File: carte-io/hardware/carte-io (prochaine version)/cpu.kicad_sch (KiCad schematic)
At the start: 24 parts, among them J3 FTSH-105-01-L-DH, SW1 SW_Push, SW2 SW_Push, U1 STM32U545VETx, X1 ASE-16.000MHZ-LC-T

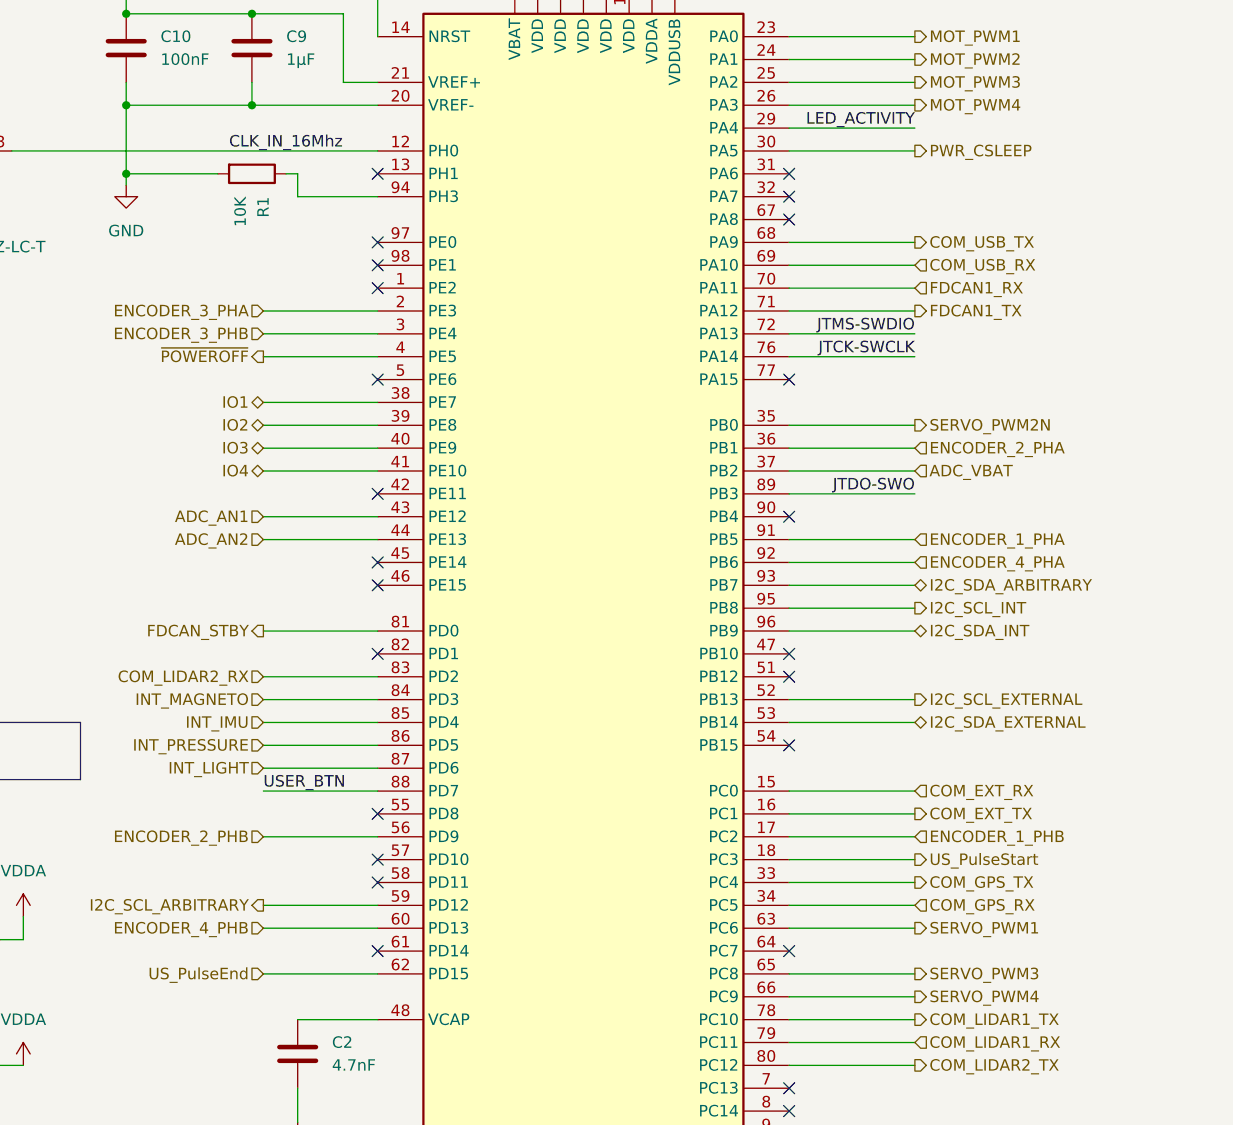
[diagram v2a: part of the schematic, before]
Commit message: WIP ajout du driver uart (marche) et du driver I2C (juste generé par chatgpt, à reprendre et tester)
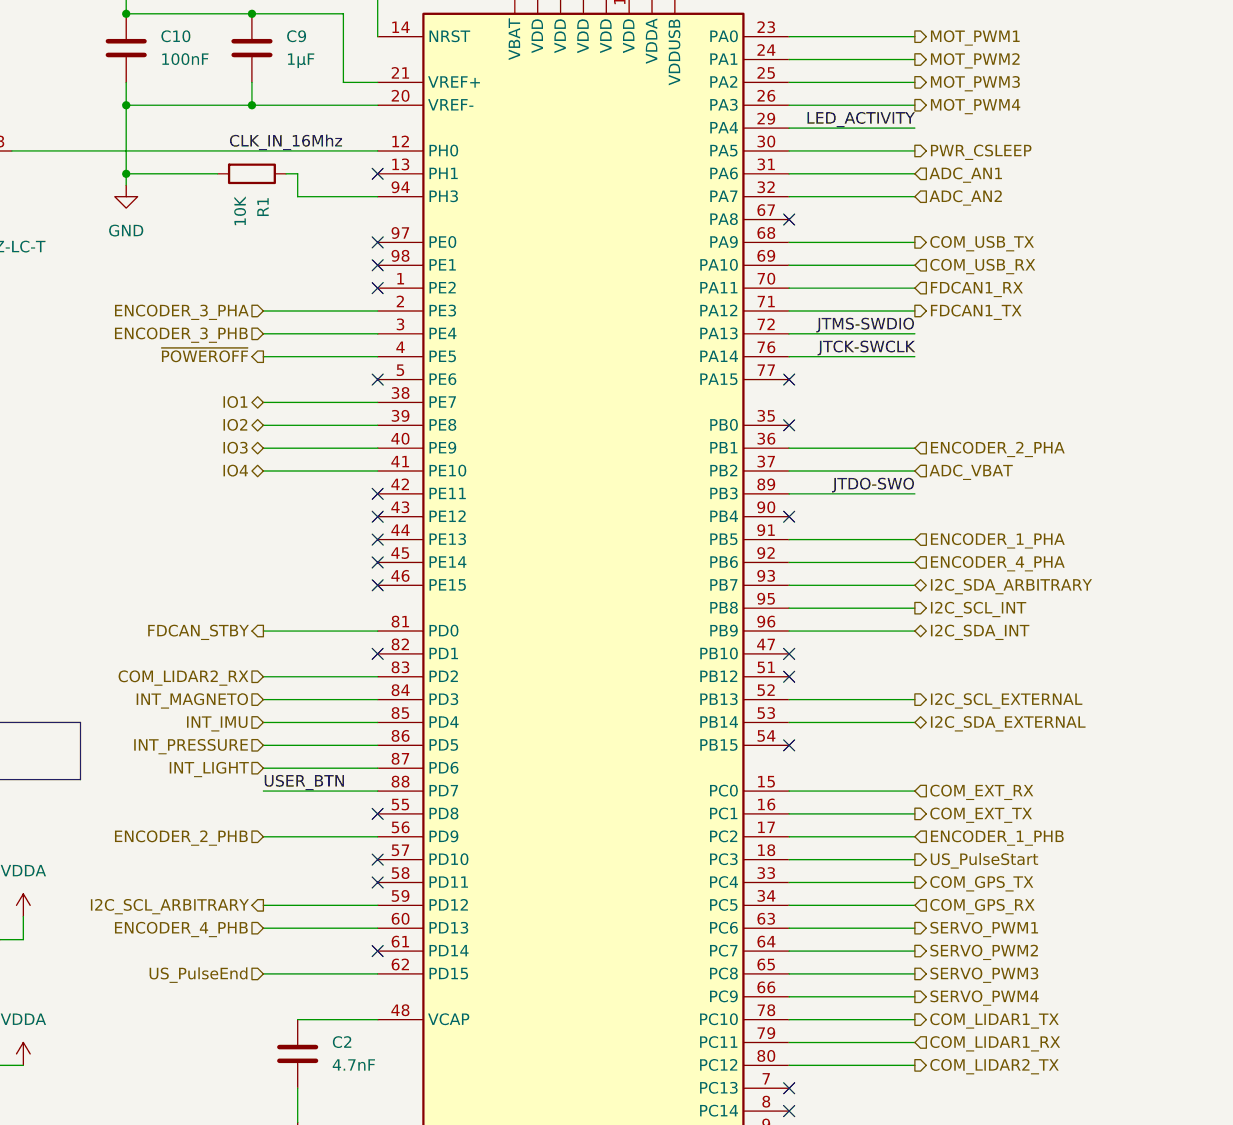
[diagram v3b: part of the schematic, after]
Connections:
- net ADC_AN1: now also U1.31 (PA6); no longer U1.43 (PE12)
- net ADC_AN2: now also U1.32 (PA7); no longer U1.44 (PE13)
- net SERVO_PWM2: now reaches U1.64 (PC7)
- net SERVO_PWM2N: no longer names the net of U1.35 (PB0)
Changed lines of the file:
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@@
-	)
-	(no_connect
-		(at 149.86 137.16)
 	)
 	(no_connect
@@
 	)
 	(no_connect
+		(at 104.14 91.44)
+	)
+	(no_connect
 		(at 104.14 127)
 	)
@@
 	)
 	(no_connect
-		(at 149.86 53.34)
-	)
-	(no_connect
 		(at 149.86 154.94)
 	)
@@
 	)
 	(no_connect
-		(at 149.86 50.8)
+		(at 149.86 78.74)
 	)
 	(no_connect
@@
 	)
 	(no_connect
+		(at 104.14 88.9)
+	)
+	(no_connect
 		(at 104.14 63.5)
 	)
@@
 	(wire
 		(pts
+			(xy 149.86 53.34) (xy 163.83 53.34)
+		)
+		(stroke
+			(width 0)
+			(type default)
+		)
+	)
+	(wire
+		(pts
 			(xy 214.63 29.21) (xy 214.63 33.02)
 		)
@@
 	(wire
 		(pts
-			(xy 149.86 78.74) (xy 163.83 78.74)
-		)
-		(stroke
-			(width 0)
-			(type default)
-		)
-	)
-	(wire
-		(pts
 			(xy 91.44 83.82) (xy 104.14 83.82)
 		)
@@
 	(wire
 		(pts
+			(xy 149.86 50.8) (xy 163.83 50.8)
+		)
+		(stroke
+			(width 0)
+			(type default)
+		)
+	)
+	(wire
+		(pts
 			(xy 50.8 175.26) (xy 50.8 177.8)
 		)
@@
 	(wire
 		(pts
-			(xy 91.44 88.9) (xy 104.14 88.9)
-		)
-		(stroke
-			(width 0)
-			(type default)
-		)
-	)
-	(wire
-		(pts
 			(xy 129.54 25.4) (xy 129.54 27.94)
 		)
@@
 	(wire
 		(pts
-			(xy 91.44 91.44) (xy 104.14 91.44)
-		)
-		(stroke
-			(width 0)
-			(type default)
-		)
-	)
-	(wire
-		(pts
 			(xy 149.86 109.22) (xy 163.83 109.22)
 		)
@@
 		(pts
 			(xy 149.86 124.46) (xy 163.83 124.46)
+		)
+		(stroke
+			(width 0)
+			(type default)
+		)
+	)
+	(wire
+		(pts
+			(xy 149.86 137.16) (xy 163.83 137.16)
 		)
 		(stroke
@@
 	(hierarchical_label "ADC_AN1"
 		(shape input)
-		(at 91.44 88.9 180)
-		(effects
-			(font
-				(size 1.27 1.27)
-			)
-			(justify right)
+		(at 163.83 50.8 0)
+		(effects
+			(font
+				(size 1.27 1.27)
+			)
+			(justify left)
 		)
 	)
@@
 	(hierarchical_label "ADC_AN2"
 		(shape input)
-		(at 91.44 91.44 180)
-		(effects
-			(font
-				(size 1.27 1.27)
-			)
-			(justify right)
+		(at 163.83 53.34 0)
+		(effects
+			(font
+				(size 1.27 1.27)
+			)
+			(justify left)
 		)
 	)
@@
 		)
 	)
-	(hierarchical_label "SERVO_PWM2N"
+	(hierarchical_label "SERVO_PWM2"
 		(shape output)
-		(at 163.83 78.74 0)
-		(effects
-			(font
+		(at 163.83 137.16 0)
+		(effects
+			(font
